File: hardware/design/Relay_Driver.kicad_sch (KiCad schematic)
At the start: 8 parts, among them K8501 G5LE-1, Q8501 2N3906, Q8502 2N3904

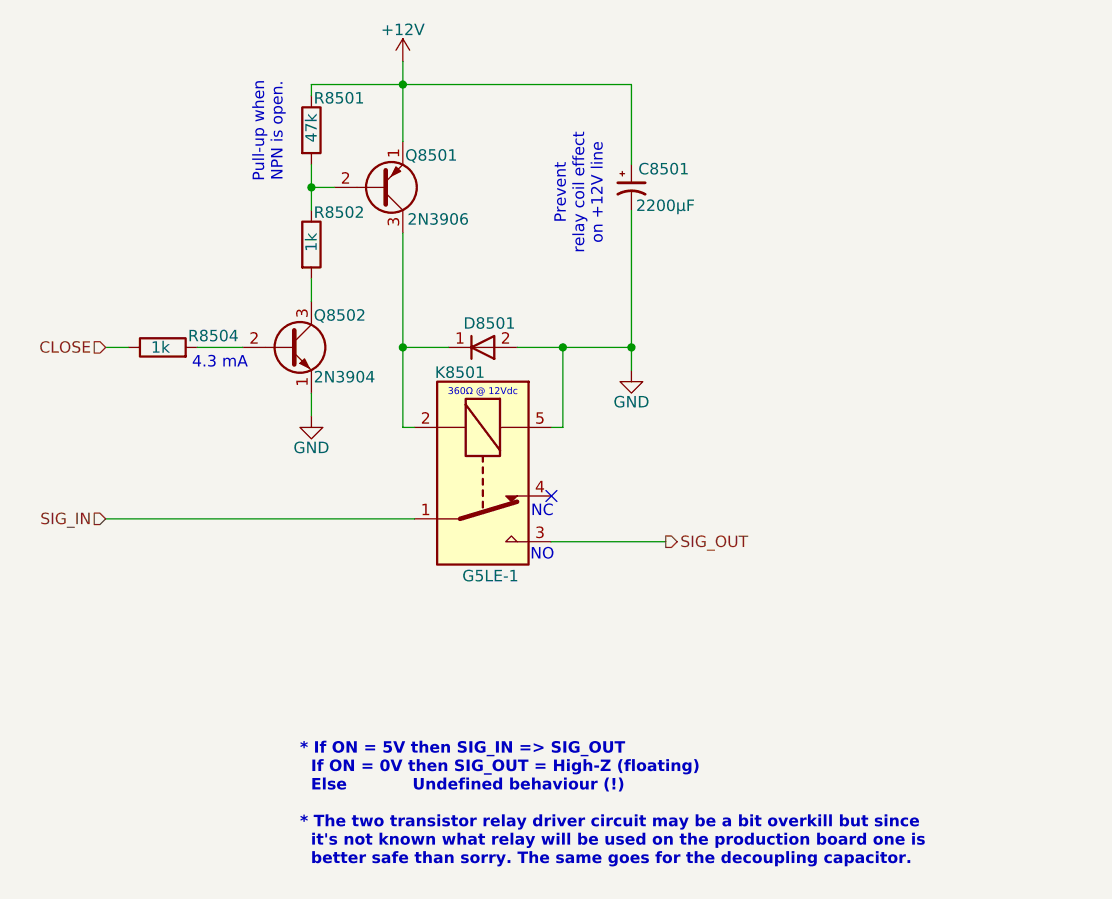
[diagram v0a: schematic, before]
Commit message: Finished proof of concept Relay_Driver
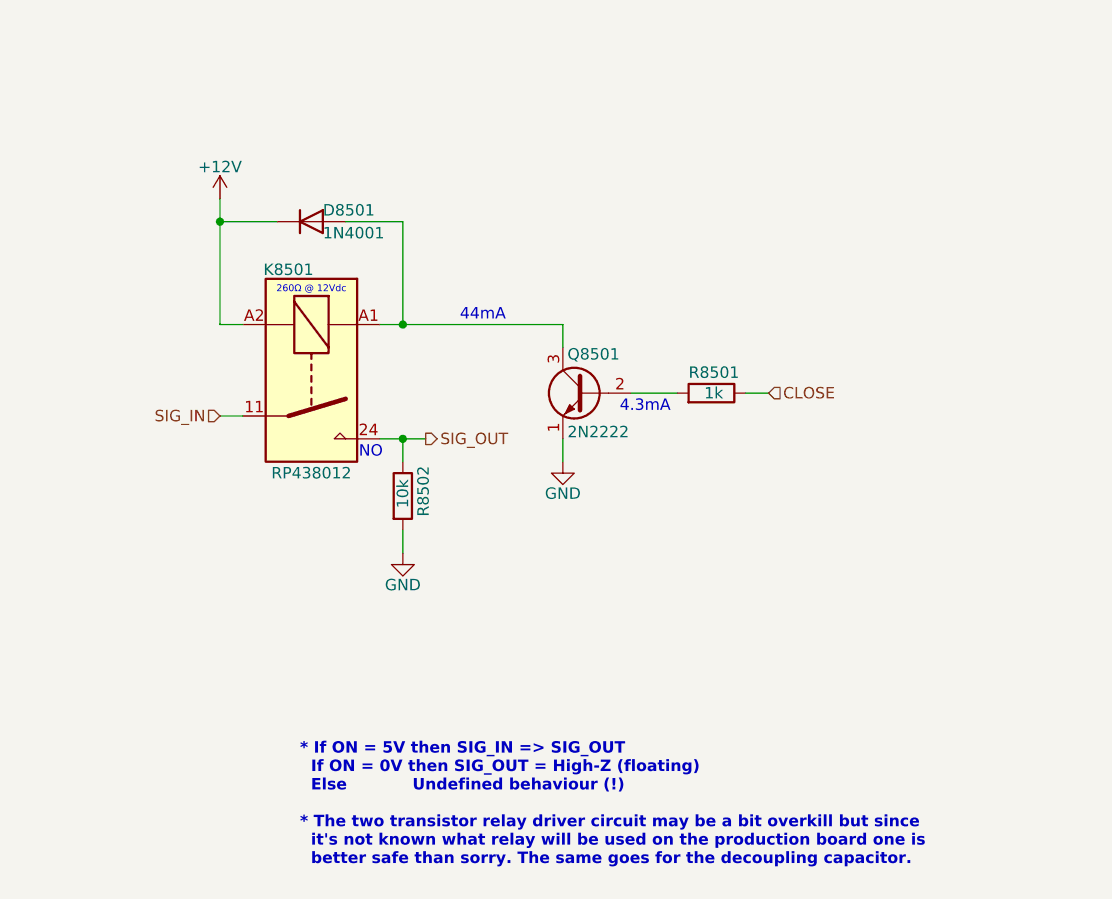
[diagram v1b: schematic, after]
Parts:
- removed C8501: 2200µF, Capacitor_THT:CP_Radial_D10.0mm_P5.00mm, symbol Device:C_Polarized_Small_US
- removed D8501: D, Diode_THT:D_5W_P10.16mm_Horizontal, symbol Simulation_SPICE:D
- removed K8501: G5LE-1, Relay_THT:Relay_SPDT_Omron-G5LE-1, symbol Relay:G5LE-1
- removed Q8501: 2N3906, Package_TO_SOT_THT:TO-92_Inline, symbol Transistor_BJT:2N3906
- removed Q8502: 2N3904, Package_TO_SOT_THT:TO-92_Inline, symbol Transistor_BJT:2N3904
- removed R8504: 1k, Resistor_THT:R_Axial_DIN0207_L6.3mm_D2.5mm_P7.62mm_Horizontal, symbol Device:R
- added D8501: 1N4001, Diode_THT:D_5W_P10.16mm_Horizontal, symbol Device:D
- added K8501: RP438012, RP438012:RP438012, symbol RP438012:RP438012-1A
- added Q8501: 2N2222, Package_TO_SOT_THT:TO-92_Inline, symbol Transistor_BJT:2N3904
- R8501: value 47k -> 1k
- R8502: value 1k -> 10k
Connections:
- net +12V: now also D8501.1 (K), K8501.A2; no longer R8501.1
- net CLOSE: now also R8501.1
- net GND: now also R8502.2, Q8501.1 (E)
- net SIG_IN: now also K8501.11
- net SIG_OUT: now also R8502.1, K8501.24
- net at R8501.2: now also Q8501.2 (B); no longer R8502.1
- new net: D8501.2 (A), K8501.A1, Q8501.3 (C)
- no-connect marks 1 -> 0
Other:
- note added: "260Ω @ 12Vdc"
- note added: "4.3mA"
- note added: "44mA"
- note removed: "360Ω @ 12Vdc"
- note removed: "4.3 mA"
- note removed: "NC"
- note removed: "Prevent relay coil effect on +12V line"
- note removed: "Pull-up when NPN is open."

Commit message: Verification board under test input impedance done (at most 3.64mA)
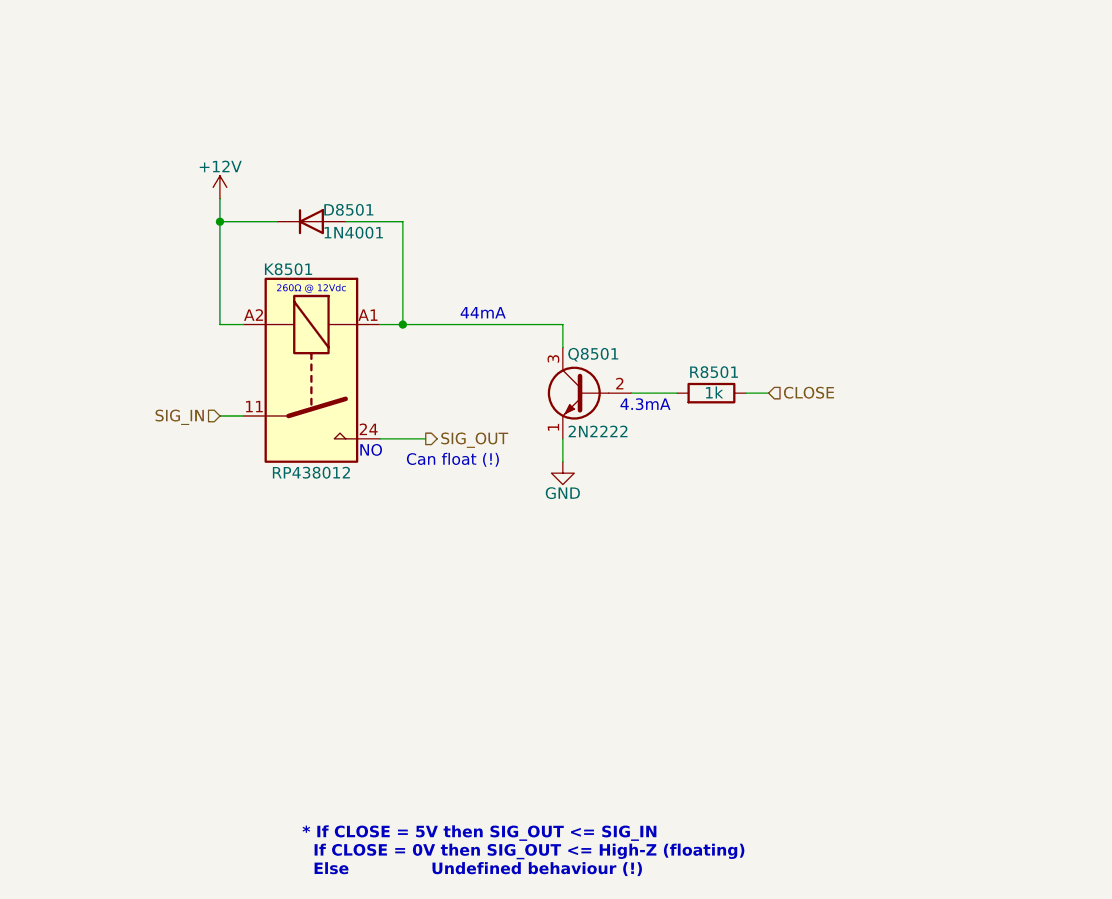
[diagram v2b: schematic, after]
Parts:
- removed R8502: 10k, Resistor_THT:R_Axial_DIN0207_L6.3mm_D2.5mm_P7.62mm_Horizontal, symbol Device:R
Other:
- note added: "* If CLOSE = 5V then SIG_OUT <= SIG_IN If CLOSE = 0V then SIG_OUT <= High-Z (floating) Else Undefined behaviour (!)"
- note added: "Can float (!)"
- note removed: "* If ON = 5V then SIG_IN => SIG_OUT If ON = 0V then SIG_OUT = High-Z (floating) Else Undefined behaviour (!) * The two transistor relay driver circuit may be a bit overkill but since it's not known what relay will be used on the production board one is better safe than sorry. The same goes for the decoupling capacitor."

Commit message: File cleanup
Added final schematics
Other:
- note added: "If CLOSE = 5V then SIG_IN => SIG_OUT If CLOSE = 0V then High-Z => SIG_OUT (floating) Else Undefined behaviour (!)"
- note removed: "* If CLOSE = 5V then SIG_OUT <= SIG_IN If CLOSE = 0V then SIG_OUT <= High-Z (floating) Else Undefined behaviour (!)"
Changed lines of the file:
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@@
 	(title_block
 		(title "VersaLogic board tester")
-		(date "2025-08-13")
-		(rev "1.0.alpha")
+		(date "2025-09-09")
+		(rev "1.0")
 		(comment 1 "Copyright (c) 2025 by Filip Pynckels & Robin Pynckels")
 	)
@@
 		)
 	)
-	(text "* If CLOSE = 5V then SIG_OUT <= SIG_IN\n  If CLOSE = 0V then SIG_OUT <= High-Z (floating)\n  Else               Undefined behaviour (!)"
+	(text "If CLOSE = 5V then SIG_IN => SIG_OUT\nIf CLOSE = 0V then High-Z => SIG_OUT (floating)\nElse               Undefined behaviour (!)"
 		(exclude_from_sim no)
 		(at 90.424 113.03 0)
